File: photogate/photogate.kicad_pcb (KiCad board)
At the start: 2 copper layers, 72.4 x 62.2 mm, 21 parts, among them P2 Jack SJ1-3525N

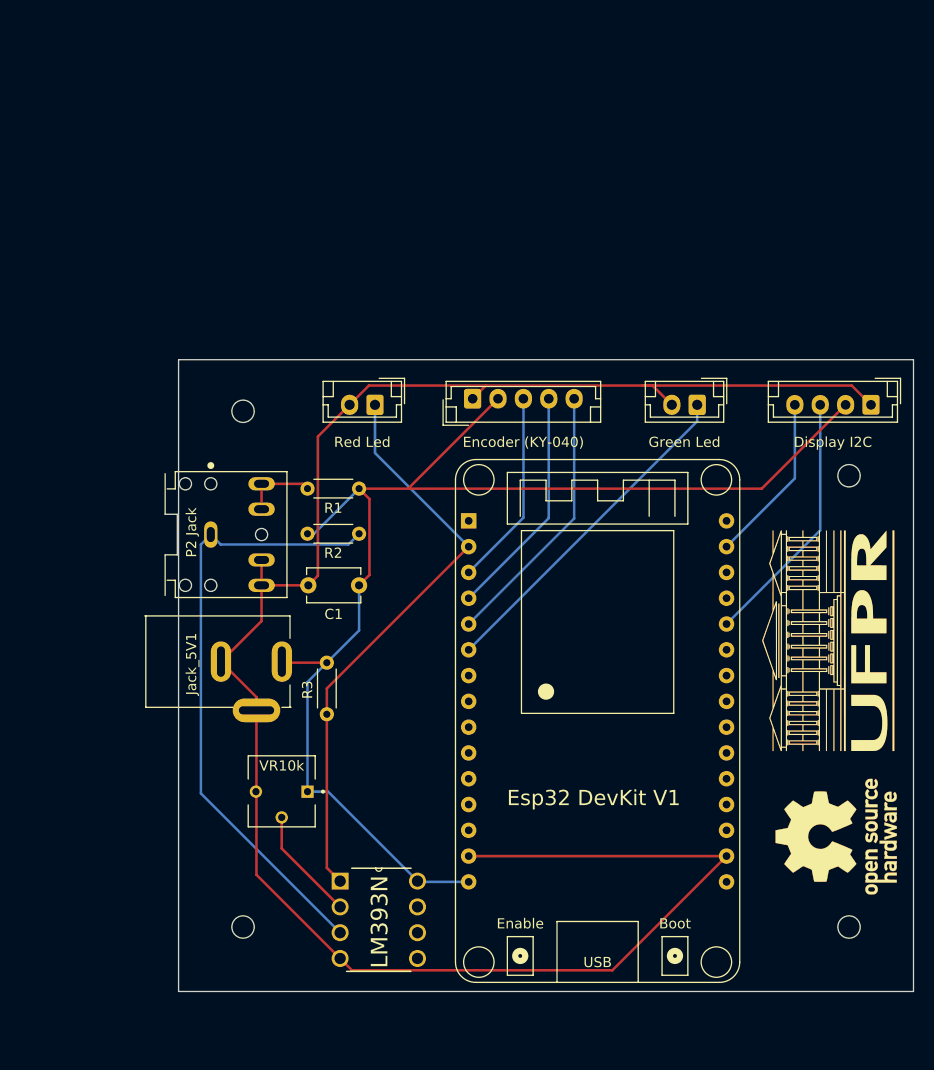
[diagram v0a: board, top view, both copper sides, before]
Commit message: Add resitor green led
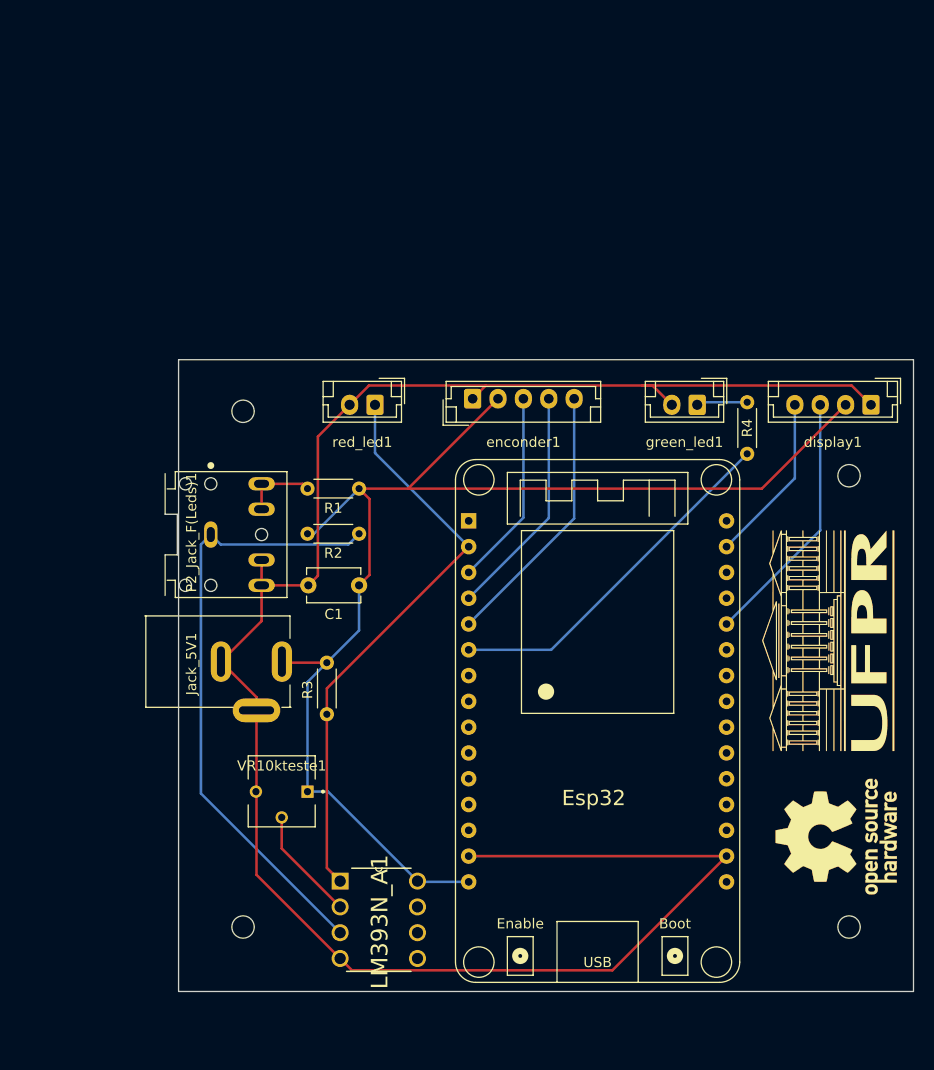
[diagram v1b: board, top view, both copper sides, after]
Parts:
- added R4: 100, Resistor_THT:R_Axial_DIN0204_L3.6mm_D1.6mm_P5.08mm_Horizontal, F.Cu at (158.5, 73.9)
- Esp32: renamed from Esp32 DevKit V1
- P2_Jack_F(Leds)1: renamed from P2 Jack
- display1: renamed from Display I2C
- enconder1: renamed from Encoder (KY-040)
- green_led1: renamed from Green Led
- red_led1: renamed from Red Led
- renumbered LM393N to LM393N_A1, VR10k to VR10kteste1
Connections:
- Esp32 pad 6: /FUNC_LED -> Net-(Esp32-Pad6)
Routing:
- net Net-(Esp32-Pad6): track 0.00 -> 35.4 mm
- net /FUNC_LED: track 33.5 -> 5.03 mm
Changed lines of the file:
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@@
   (net 31 "Net-(LM393N_A1-Pad2)")
   (net 32 "Net-(P2_Jack_F(Leds)1-Pad11)")
+  (net 33 "Net-(Esp32-Pad6)")
   (footprint "MyFootprints:TRIM_3362P-1-103" (layer "F.Cu")
     (at 112.649 107.188 180)
@@
     (property "Sheetname" "")
     (attr through_hole)
-    (fp_text reference "VR10k" (at 0 2.54) (layer "F.SilkS")
+    (fp_text reference "VR10kteste1" (at 0 2.54) (layer "F.SilkS")
       (effects (font (size 1.002756 1.002756) (thickness 0.15)))
     )
@@
     (property "Sheetname" "")
     (attr through_hole)
-    (fp_text reference "LM393N" (at 0.127 -0.508 90) (layer "F.SilkS")
+    (fp_text reference "LM393N_A1" (at 0.127 -0.508 90) (layer "F.SilkS")
       (effects (font (size 1.641157 1.641157) (thickness 0.15)))
     )
@@
     (property "Sheetname" "")
     (attr through_hole)
-    (fp_text reference "Green Led" (at 1.25 -3.683) (layer "F.SilkS")
+    (fp_text reference "green_led1" (at 1.25 -3.683) (layer "F.SilkS")
       (effects (font (size 1 1) (thickness 0.15)))
     )
@@
     (property "Sheetname" "")
     (attr through_hole)
-    (fp_text reference "Display I2C" (at 3.75 -3.683) (layer "F.SilkS")
+    (fp_text reference "display1" (at 3.75 -3.683) (layer "F.SilkS")
       (effects (font (size 1 1) (thickness 0.15)))
     )
@@
     (property "Sheetname" "")
     (attr smd)
-    (fp_text reference "Esp32 DevKit V1" (at -0.381 27.305) (layer "F.SilkS")
+    (fp_text reference "Esp32" (at -0.381 27.305) (layer "F.SilkS")
       (effects (font (size 1.5 1.5) (thickness 0.3)))
     )
@@
       (net 7 "/CLK") (pinfunction "IO35") (pintype "input"))
     (pad "6" thru_hole circle locked (at -12.7 12.7) (size 1.524 1.524) (drill 0.762) (layers *.Cu *.Mask)
-      (net 8 "/FUNC_LED") (pinfunction "IO32") (pintype "bidirectional"))
+      (net 33 "Net-(Esp32-Pad6)") (pinfunction "IO32") (pintype "bidirectional"))
     (pad "7" thru_hole circle locked (at -12.7 15.24) (size 1.524 1.524) (drill 0.762) (layers *.Cu *.Mask)
       (net 12 "unconnected-(Esp32-Pad7)") (pinfunction "IO33") (pintype "bidirectional"))
@@
     (property "Sheetname" "")
     (attr through_hole)
-    (fp_text reference "Red Led" (at 1.25 -3.683) (layer "F.SilkS")
+    (fp_text reference "red_led1" (at 1.25 -3.683) (layer "F.SilkS")
       (effects (font (size 1 1) (thickness 0.15)))
     )
@@
     (property "Sheetname" "")
     (attr through_hole)
-    (fp_text reference "Encoder (KY-040)" (at 5 4.283) (layer "F.SilkS")
+    (fp_text reference "enconder1" (at 5 4.283) (layer "F.SilkS")
       (effects (font (size 1 1) (thickness 0.15)))
     )
@@
     (pad "" np_thru_hole circle (at 0 0) (size 2.2 2.2) (drill 2.2) (layers *.Cu *.Mask))
   )
+  (footprint "Resistor_THT:R_Axial_DIN0204_L3.6mm_D1.6mm_P5.08mm_Horizontal" (layer "F.Cu")
+    (at 158.496 73.914 90)
+    (descr "Resistor, Axial_DIN0204 series, Axial, Horizontal, pin pitch=5.08mm, 0.167W, length*diameter=3.6*1.6mm^2, http://cdn-reichelt.de/documents/datenblatt/B400/1_4W%23YAG.pdf")
+    (tags "Resistor Axial_DIN0204 series Axial Horizontal pin pitch 5.08mm 0.167W length 3.6mm diameter 1.6mm")
+    (property "Sheetfile" "photogate.kicad_sch")
+    (property "Sheetname" "")
+    (attr through_hole)
+    (fp_text reference "R4" (at 2.54 0 90) (layer "F.SilkS")
+      (effects (font (size 1 1) (thickness 0.15)))
+    )
+    (fp_text value "100" (at 2.54 1.92 90) (layer "F.Fab")
+      (effects (font (size 1 1) (thickness 0.15)))
+    )
+    (fp_text user "${REFERENCE}" (at 2.54 0 90) (layer "F.Fab")
+      (effects (font (size 0.72 0.72) (thickness 0.108)))
+    )
+    (fp_line (start 0.62 -0.92) (end 4.46 -0.92) (layer "F.SilkS") (width 0.12))
+    (fp_line (start 0.62 0.92) (end 4.46 0.92) (layer "F.SilkS") (width 0.12))
+    (fp_line (start 6.03 1.05) (end 6.03 -1.05) (layer "F.CrtYd") (width 0.05))
+    (fp_line (start -0.95 1.05) (end 6.03 1.05) (layer "F.CrtYd") (width 0.05))
+    (fp_line (start -0.95 -1.05) (end -0.95 1.05) (layer "F.CrtYd") (width 0.05))
+    (fp_line (start 6.03 -1.05) (end -0.95 -1.05) (layer "F.CrtYd") (width 0.05))
+    (fp_line (start 0.74 0.8) (end 4.34 0.8) (layer "F.Fab") (width 0.1))
+    (fp_line (start 0 0) (end 0.74 0) (layer "F.Fab") (width 0.1))
+    (fp_line (start 0.74 -0.8) (end 0.74 0.8) (layer "F.Fab") (width 0.1))
+    (fp_line (start 5.08 0) (end 4.34 0) (layer "F.Fab") (width 0.1))
+    (fp_line (start 4.34 0.8) (end 4.34 -0.8) (layer "F.Fab") (width 0.1))
+    (fp_line (start 4.34 -0.8) (end 0.74 -0.8) (layer "F.Fab") (width 0.1))
+    (pad "1" thru_hole circle (at 0 0 90) (size 1.4 1.4) (drill 0.7) (layers *.Cu *.Mask)
+      (net 33 "Net-(Esp32-Pad6)") (pintype "passive"))
+    (pad "2" thru_hole oval (at 5.08 0 90) (size 1.4 1.4) (drill 0.7) (layers *.Cu *.Mask)
+      (net 8 "/FUNC_LED") (pintype "passive"))
+    (model "${KICAD6_3DMODEL_DIR}/Resistor_THT.3dshapes/R_Axial_DIN0204_L3.6mm_D1.6mm_P5.08mm_Horizontal.wrl"
+      (offset (xyz 0 0 0))
+      (scale (xyz 1 1 1))
+      (rotate (xyz 0 0 0))
+    )
+  )
   (footprint "MyFootprints:CUI_SJ1-3525N" (layer "F.Cu")
     (at 105.664 81.868)
@@
     (property "Sheetname" "")
     (attr through_hole)
-    (fp_text reference "P2 Jack" (at -1.905 -0.207 90) (layer "F.SilkS")
+    (fp_text reference "P2_Jack_F(Leds)1" (at -1.905 -0.207 90) (layer "F.SilkS")
       (effects (font (size 1.000457 1.000457) (thickness 0.15)))
     )
@@
   (segment (start 141.454833 80.287167) (end 131.064 90.678) (width 0.25) (layer "B.Cu") (net 7))
   (segment (start 141.454833 68.488) (end 141.454833 80.287167) (width 0.25) (layer "B.Cu") (net 7))
-  (segment (start 153.573166 69.088) (end 153.573166 70.708834) (width 0.25) (layer "B.Cu") (net 8))
-  (segment (start 153.573166 70.708834) (end 131.064 93.218) (width 0.25) (layer "B.Cu") (net 8))
+  (segment (start 153.827166 68.834) (end 153.573166 69.088) (width 0.25) (layer "B.Cu") (net 8))
+  (segment (start 158.496 68.834) (end 153.827166 68.834) (width 0.25) (layer "B.Cu") (net 8))
   (segment (start 106.639001 82.843001) (end 119.213999 82.843001) (width 0.25) (layer "B.Cu") (net 9))
   (segment (start 105.664 81.868) (end 106.639001 82.843001) (width 0.25) (layer "B.Cu") (net 9))
@@
   (segment (start 110.664 76.868) (end 114.714 76.868) (width 0.25) (layer "F.Cu") (net 32))
   (segment (start 114.714 76.868) (end 115.189 77.343) (width 0.25) (layer "F.Cu") (net 32))
+  (segment (start 139.192 93.218) (end 158.496 73.914) (width 0.25) (layer "B.Cu") (net 33))
+  (segment (start 131.064 93.218) (end 139.192 93.218) (width 0.25) (layer "B.Cu") (net 33))
   (group "" (id 14e08493-23b3-4c49-bdad-c9907105a379)
     (members

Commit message: Melhoras na placa
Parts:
- removed the REF** at (167.3, 111.6)
- removed the REF** at (168.5, 76.1)
- removed the REF** at (168.5, 120.5)
- removed the UFPR at (166.2, 92.1)
- added REF**: MountingHole_2.2mm_M2, MountingHole:MountingHole_2.2mm_M2, F.Cu at (169.5, 74.9)
- added REF**: MountingHole_2.2mm_M2, MountingHole:MountingHole_2.2mm_M2, F.Cu at (169.5, 120.7)
- Esp32 DevKit V1: renamed from Esp32
- Green Led: renamed from green_led1
- Inferior Esquerdo: renamed from REF**
- Jack 5V1: renamed from Jack_5V1
- P2 Jack F: renamed from P2_Jack_F(Leds)1
- Red Led: renamed from red_led1
- moved Red Led 22.1 mm to (143.9, 67.6)
- moved R4 10.3 mm to (148.3, 72.7)
- moved Green Led 2.24 mm to (155.3, 67.6)
- moved Display 1.75 mm to (171.6, 67.6)
- moved Encoder 1.37 mm to (132.5, 67.6), turned to 180 degrees
- moved REF** 0.18 mm to (108.7, 69.8)
- renumbered display1 to Display, enconder1 to Encoder, LM393N_A1 to LM393N, VR10kteste1 to VR10k
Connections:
- Esp32 DevKit V1 pad 17: GND -> unconnected-(Esp32-Pad17)
- Green Led pad 1: /FUNC_LED -> GND
- Green Led pad 2: GND -> /FUNC_LED
- Red Led pad 1: /D0 -> GND
- Red Led pad 2: GND -> /D0
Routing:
- net GND: track 197.9 -> 143.7 mm
- net Net-(C1-Pad1): track 127.6 -> 114.5 mm
- net Net-(Esp32-Pad6): track 35.4 -> 27.6 mm
- net /D0: track 57.1 -> 59.0 mm
- net /SCL: track 16.8 -> 18.6 mm
- net /SDA: track 25.4 -> 27.3 mm
- net /FUNC_LED: track 5.03 -> 4.50 mm
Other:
- board size 72.4 x 62.2 mm -> 72.8 x 62.1 mm

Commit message: add intruções na PCI
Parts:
- added P2 3poles: LOGO, simbolos:P2_3poles, F.Cu at (111.5, 72.8)
- renumbered VR10k to VR
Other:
- board text added: "CLK"
- board text added: "DT"
- board text added: "Feito por: Marcio Ap. Bulla Jr. Código Fonte: github.com/MarcioBulla/Cronometro-Optico"
- board text added: "GND"
- board text added: "P2 Esterio"
- board text added: "POS"
- board text added: "R led"
- board text added: "SCL"
- board text added: "SDA"
- board text added: "SW"
- board text added: "T led"
- board text added: "VCC"
- board text added: "Versão: 1.0"
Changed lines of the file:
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@@
     (property "Sheetname" "")
     (attr through_hole)
-    (fp_text reference "VR10k" (at 0 2.54) (layer "F.SilkS")
+    (fp_text reference "VR" (at 0 2.54) (layer "F.SilkS")
       (effects (font (size 1.002756 1.002756) (thickness 0.15)))
     )
@@
     (property "Sheetname" "")
     (attr through_hole)
-    (fp_text reference "Green Led" (at 1.25 -3.683) (layer "F.SilkS")
+    (fp_text reference "Green Led" (at 1.25 -4.78) (layer "F.SilkS")
       (effects (font (size 1 1) (thickness 0.15)))
     )
@@
     (property "Sheetname" "")
     (attr through_hole)
-    (fp_text reference "Display" (at 3.75 -3.683) (layer "F.SilkS")
+    (fp_text reference "Display" (at 3.75 -4.78) (layer "F.SilkS")
       (effects (font (size 1 1) (thickness 0.15)))
     )
@@
     (property "Sheetname" "")
     (attr through_hole)
-    (fp_text reference "Red Led" (at 1.25 -3.683) (layer "F.SilkS")
+    (fp_text reference "Red Led" (at 1.25 -4.78) (layer "F.SilkS")
       (effects (font (size 1 1) (thickness 0.15)))
     )
@@
     (property "Sheetname" "")
     (attr through_hole)
-    (fp_text reference "Encoder" (at 5.842 -3.556) (layer "F.SilkS")
+    (fp_text reference "Encoder" (at 5.842 -4.78) (layer "F.SilkS")
       (effects (font (size 1 1) (thickness 0.15)))
     )
@@
     )
   )
+  (footprint "simbolos:P2_3poles" (layer "F.Cu")
+    (at 111.5314 72.771)
+    (attr board_only exclude_from_pos_files exclude_from_bom)
+    (fp_text reference "P2 3poles" (at -0.2286 -4.3688) (layer "F.SilkS") hide
+      (effects (font (size 1.524 1.524) (thickness 0.3)))
+    )
+    (fp_text value "LOGO" (at 0.75 0) (layer "F.SilkS") hide
+      (effects (font (size 1.524 1.524) (thickness 0.3)))
+    )
+    (fp_rect (start 3.6195 -1.4224) (end -0.1143 1.1684) (layer "F.SilkS") (width 0.2) (fill none))
+    (fp_rect (start 9.2837 -1.8034) (end 3.5941 1.6256) (layer "F.SilkS") (width 0.2) (fill none))
+    (fp_rect (start -0.1143 -1.4224) (end -3.8481 1.1684) (layer "F.SilkS") (width 0.2) (fill none))
+    (fp_poly (pts
+        (xy -3.8481 1.1684)
+        (xy -5.1054 1.1684)
+        (xy -5.6134 0.6858)
+        (xy -7.6454 1.1684)
+        (xy -8.9408 0.4318)
+        (xy -8.9408 -0.635)
+        (xy -7.6454 -1.3716)
+        (xy -5.588 -0.889)
+        (xy -5.1054 -1.4224)
+        (xy -3.8481 -1.4224)
+      ) (layer "F.SilkS") (width 0.2) (fill none))
+  )
   (footprint "MountingHole:MountingHole_2.2mm_M2" (layer "F.Cu")
     (at 108.712 69.85)
@@
   )
   (gr_rect (start 102.108 64.77) (end 174.879 126.873) (layer "Edge.Cuts") (width 0.1) (fill none))
+  (gr_text "Feito por: \nMarcio Ap. Bulla Jr.\n\nCódigo Fonte: \ngithub.com/MarcioBulla/Cronometro-Optico\n" (at 139.7 74.93 90) (layer "B.SilkS")
+    (effects (font (size 1.5 1.5) (thickness 0.3) italic) (justify left mirror))
+  )
+  (gr_text "GND" (at 171.6275 70.485) (layer "F.SilkS")
+    (effects (font (size 0.75 0.75) (thickness 0.15)))
+  )
+  (gr_text "Versão: 1.0" (at 124.46 99.695 90) (layer "F.SilkS")
+    (effects (font (size 2 2) (thickness 0.3)))
+  )
+  (gr_text "P2 \nEsterio" (at 117.8814 72.644) (layer "F.SilkS")
+    (effects (font (size 0.75 0.75) (thickness 0.15)))
+  )
+  (gr_text "T led" (at 109.6264 72.644) (layer "F.SilkS")
+    (effects (font (size 0.75 0.75) (thickness 0.15)))
+  )
+  (gr_text "POS" (at 152.754332 70.485) (layer "F.SilkS")
+    (effects (font (size 0.75 0.75) (thickness 0.15)))
+  )
+  (gr_text "GND" (at 143.881166 70.485) (layer "F.SilkS")
+    (effects (font (size 0.75 0.75) (thickness 0.15)))
+  )
+  (gr_text "POS" (at 141.381166 70.485) (layer "F.SilkS")
+    (effects (font (size 0.75 0.75) (thickness 0.15)))
+  )
+  (gr_text "GND" (at 155.254332 70.485) (layer "F.SilkS")
+    (effects (font (size 0.75 0.75) (thickness 0.15)))
+  )
+  (gr_text "DT" (at 125.008 70.485) (layer "F.SilkS")
+    (effects (font (size 0.75 0.75) (thickness 0.15)))
+  )
+  (gr_text "VCC" (at 169.1275 70.485) (layer "F.SilkS")
+    (effects (font (size 0.75 0.75) (thickness 0.15)))
+  )
+  (gr_text "R led" (at 105.1814 72.644) (layer "F.SilkS")
+    (effects (font (size 0.75 0.75) (thickness 0.15)))
+  )
+  (gr_text "VCC" (at 130.008 70.485) (layer "F.SilkS")
+    (effects (font (size 0.75 0.75) (thickness 0.15)))
+  )
+  (gr_text "GND" (at 113.4364 72.6821) (layer "F.SilkS")
+    (effects (font (size 0.75 0.75) (thickness 0.15)))
+  )
+  (gr_text "SDA" (at 166.6275 70.485) (layer "F.SilkS")
+    (effects (font (size 0.75 0.75) (thickness 0.15)))
+  )
+  (gr_text "CLK" (at 122.508 70.485) (layer "F.SilkS")
+    (effects (font (size 0.75 0.75) (thickness 0.15)))
+  )
+  (gr_text "SCL" (at 164.1275 70.485) (layer "F.SilkS")
+    (effects (font (size 0.75 0.75) (thickness 0.15)))
+  )
+  (gr_text "SW\n" (at 127.508 70.485) (layer "F.SilkS")
+    (effects (font (size 0.75 0.75) (thickness 0.15)))
+  )
+  (gr_text "GND" (at 132.508 70.485) (layer "F.SilkS")
+    (effects (font (size 0.75 0.75) (thickness 0.15)))
+  )
   (segment (start 130.002 67.61) (end 120.269 77.343) (width 0.25) (layer "F.Cu") (net 1))
   (segment (start 169.1275 67.61) (end 167.8025 66.285) (width 0.25) (layer "F.Cu") (net 1))
@@
       8d59341b-cc34-4cd2-b2fa-e3f1940fb7c6
       cf235b1a-3e32-4859-875c-61ee6e39efee
+      dfcf44aa-b0a3-4d3f-b1e2-528db8c8e6b3
+    )
+  )
+  (group "" (id 776ef48e-87f1-479e-92c7-d3cd67a12d6d)
+    (members
+      1e3e007f-6e91-4eac-821e-04406401d5b4
+      2324194c-9491-4113-bdc3-5d6b9cea09f0
+      9e019146-71aa-48b1-920d-16ca451ee684
+      b39ca0d6-ecda-452c-915c-0ad1c646fd95
+      edbdacf4-8d8e-4ac9-b84c-f3b4bc60f97b
+    )
+  )
+  (group "" (id 79ff3c98-da62-4fd9-8315-a621f1adddae)
+    (members
+      13fc947e-c316-4848-8638-bac898e642de
+      7242458e-de4a-4703-9f65-eb4e4e3b1860
+      cc5583d6-f71c-4920-8980-bce7901e3439
+      e4eba0cb-6e45-4692-80f7-56110b8d29d2
+    )
+  )
+  (group "" (id 9809aebd-4437-43bd-bc12-84fe6c48282c)
+    (members
+      3523918a-ab11-4ed7-8bfe-014389521ac7
+      5b56577f-ab79-4da6-86ad-11d73eb0c53c
+    )
+  )
+  (group "" (id b3502b2a-9526-4acc-a90d-83b2a38c23b8)
+    (members
+      60686e62-2de6-4653-9a56-94bacd486c95
+      b1ced882-fd8e-4f1e-a533-caa6ceff2d6a
+      d8137dce-209a-4ccb-b9c4-d8d2456a525f
+      ed2d5fe5-15c4-4e22-92c7-83d4f906b399
+      fdc48a40-3465-40b7-a476-c76bdefed65d
+    )
+  )
+  (group "" (id bf4e867e-2f05-4454-be63-b109659adc37)
+    (members
+      3a3f8cd4-b998-4c36-93ac-97b4b81c623a
+      55a3305e-77ba-45ce-9ab3-ab4fb7292ef2
     )
   )
